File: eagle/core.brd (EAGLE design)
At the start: 41.9 x 19.7 mm, 28 parts, among them T1 BC846, T2 BC846, T3 BC846, T4 BC846

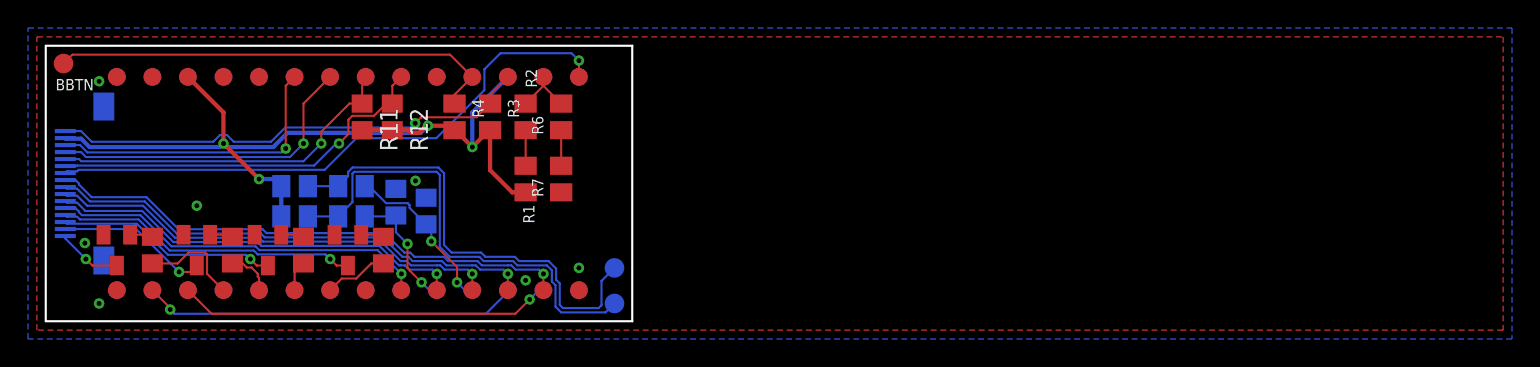
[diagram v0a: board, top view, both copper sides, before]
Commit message: Fixed ffc connector dimensions
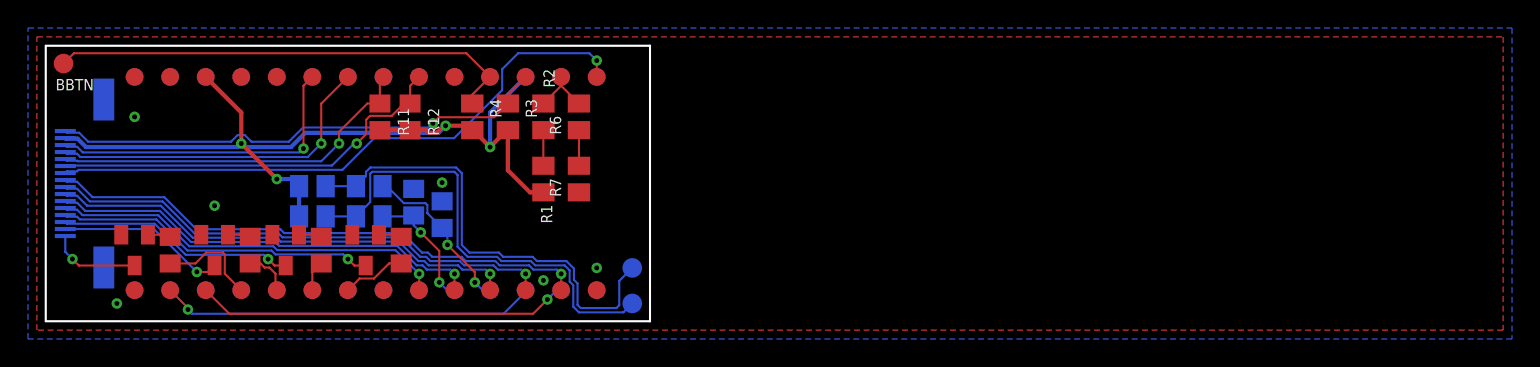
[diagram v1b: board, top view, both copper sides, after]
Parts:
- moved C2 1.27 mm to (26.3, 8.51)
- moved R1 1.27 mm to (35.6, 10.2)
- moved R2 1.27 mm to (35.6, 14.6)
- moved R3 1.27 mm to (33.0, 14.6)
- moved R6 1.27 mm to (38.1, 14.6)
- moved R7 1.27 mm to (38.1, 10.2)
- moved R15 1.27 mm to (8.89, 5.08)
- moved R10 1.27 mm to (23.1, 7.49)
- moved R11 1.27 mm to (23.9, 14.6)
- moved R12 1.27 mm to (26.0, 14.6)
- moved R16 1.27 mm to (14.6, 5.08)
- moved R17 1.27 mm to (19.7, 5.08)
- moved R18 1.27 mm to (25.4, 5.08)
- moved R4 1.27 mm to (30.5, 14.6)
- moved R5 1.27 mm to (23.1, 9.65)
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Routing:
- net L1-: track 4.66 -> 6.49 mm
- net BBTN: track 32.6 -> 33.9 mm
- net SDA: track 28.0 -> 29.3 mm
- net TFTCS: track 35.4 -> 36.6 mm
- net DC: track 32.6 -> 33.9 mm
- net L2-: track 10.9 -> 12.1 mm
- net SCL: track 25.5 -> 26.8 mm
- net LRCL: track 23.1 -> 24.4 mm
- net L4-: track 21.7 -> 23.0 mm
- net L3-: track 15.8 -> 17.0 mm
- net BCLK: track 21.5 -> 22.7 mm
- net SCK: track 42.5 -> 43.8 mm
- net PBTN: track 34.6 -> 35.9 mm
- net DOUT: track 29.9 -> 31.1 mm
- net 3V: track 63.1 -> 64.3 mm
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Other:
- board size 41.9 x 19.7 mm -> 43.2 x 19.7 mm

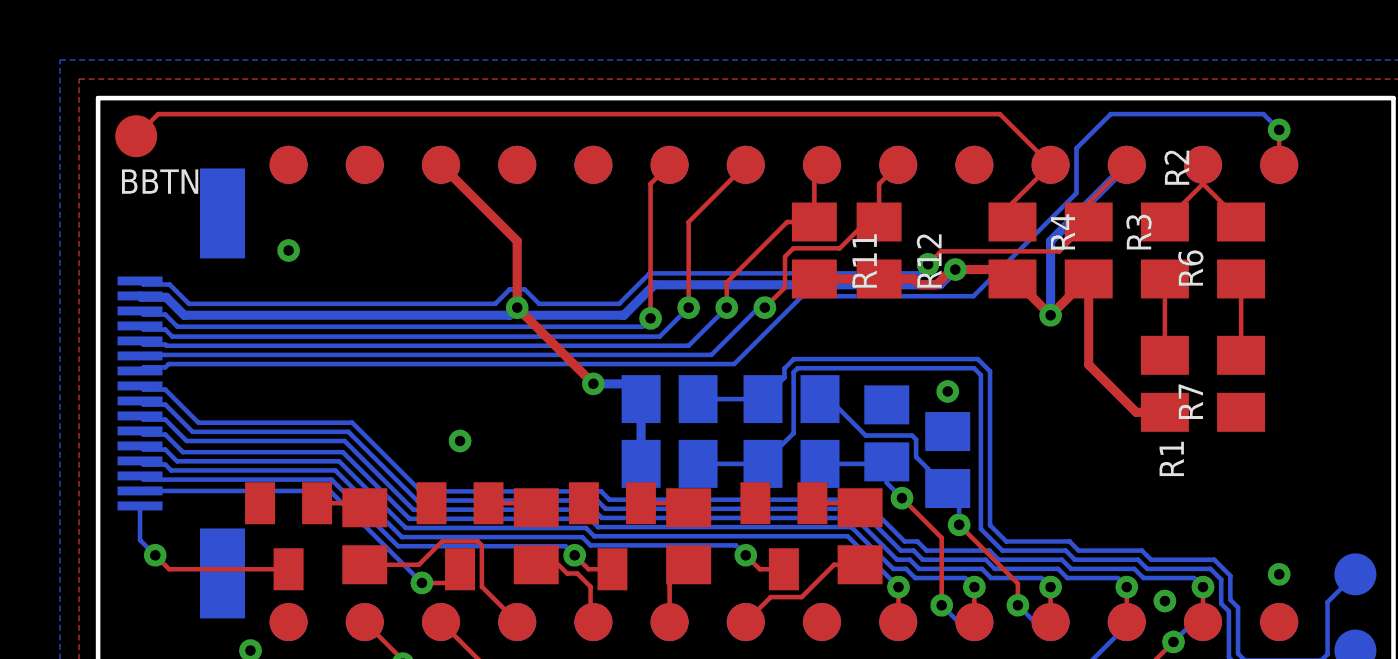
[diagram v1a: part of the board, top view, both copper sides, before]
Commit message: Added capacitor between 3v and gnd on core pcb
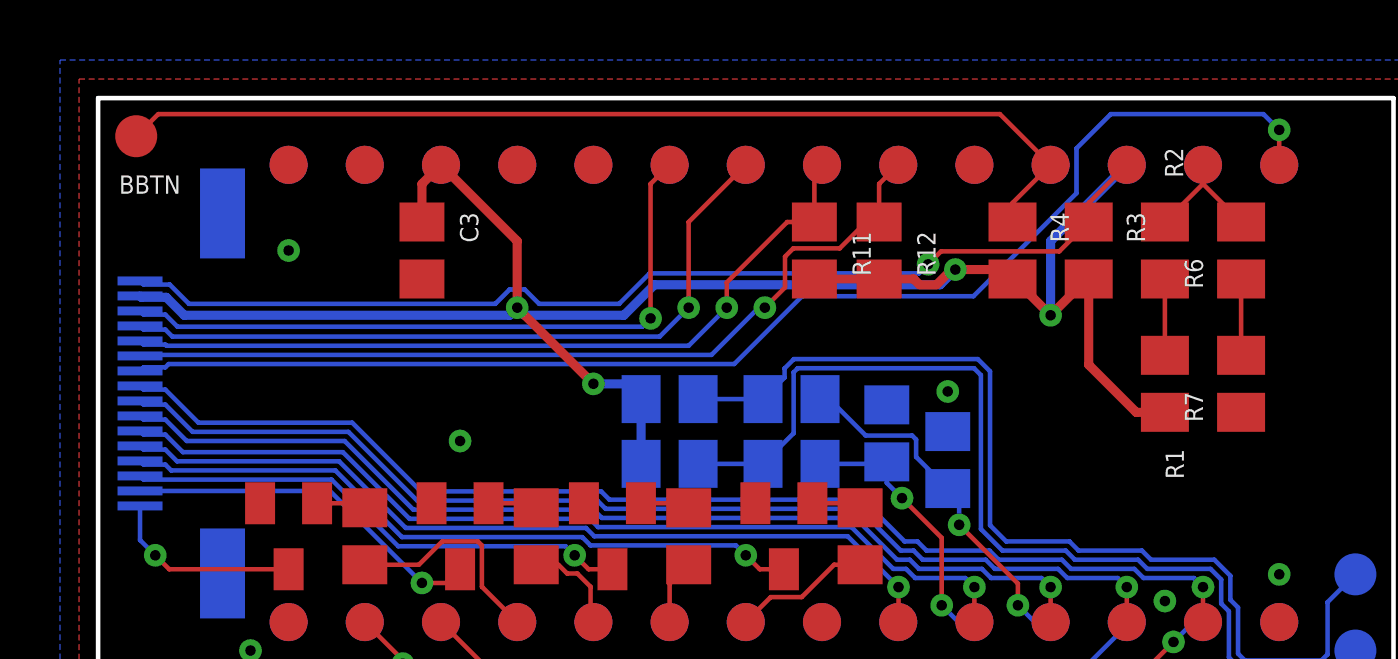
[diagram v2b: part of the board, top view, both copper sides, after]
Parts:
- added C3: 0.1u, resistor:C0805
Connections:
- net 3V: now also C3.1
- net GND: now also C3.2
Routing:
- net 3V: track 64.3 -> 66.5 mm
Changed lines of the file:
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@@
 <elements>
 <element name="R5" library="resistor" library_urn="urn:adsk.eagle:library:348" package="M0805" package3d_urn="urn:adsk.eagle:package:23556/2" value="10k" x="23.114" y="9.652" smashed="yes" rot="MR0">
-<attribute name="NAME" x="19.304" y="10.287" size="0.8128" layer="26" rot="MR180"/>
+<attribute name="NAME" x="19.304" y="10.287" size="0.6096" layer="26" rot="MR180"/>
 <attribute name="VALUE" x="24.384" y="7.112" size="1.27" layer="28" rot="MR0"/>
 </element>
 <element name="R8" library="resistor" library_urn="urn:adsk.eagle:library:348" package="M0805" package3d_urn="urn:adsk.eagle:package:23556/2" value="10k" x="19.05" y="9.652" smashed="yes" rot="MR0">
-<attribute name="NAME" x="19.685" y="10.922" size="0.8128" layer="26" rot="MR0"/>
+<attribute name="NAME" x="19.685" y="10.922" size="0.6096" layer="26" rot="MR0"/>
 <attribute name="VALUE" x="20.32" y="7.112" size="1.27" layer="28" rot="MR0"/>
 </element>
 <element name="R9" library="resistor" library_urn="urn:adsk.eagle:library:348" package="M0805" package3d_urn="urn:adsk.eagle:package:23556/2" value="10k" x="19.05" y="7.493" smashed="yes" rot="MR0">
-<attribute name="NAME" x="21.59" y="10.668" size="0.8128" layer="26" rot="MR180"/>
+<attribute name="NAME" x="21.59" y="10.668" size="0.6096" layer="26" rot="MR180"/>
 <attribute name="VALUE" x="20.32" y="4.953" size="1.27" layer="28" rot="MR0"/>
 </element>
 <element name="R10" library="resistor" library_urn="urn:adsk.eagle:library:348" package="M0805" package3d_urn="urn:adsk.eagle:package:23556/2" value="10k" x="23.114" y="7.493" smashed="yes" rot="MR0">
-<attribute name="NAME" x="24.384" y="11.303" size="0.8128" layer="26" rot="MR0"/>
+<attribute name="NAME" x="24.384" y="11.303" size="0.6096" layer="26" rot="MR0"/>
 <attribute name="VALUE" x="24.384" y="4.953" size="1.27" layer="28" rot="MR0"/>
 </element>
 <element name="C1" library="resistor" library_urn="urn:adsk.eagle:library:348" package="C0805" package3d_urn="urn:adsk.eagle:package:23617/2" value="0.1u" x="28.321" y="7.62" smashed="yes" rot="MR90">
-<attribute name="NAME" x="28.321" y="3.81" size="0.8128" layer="26" rot="MR90"/>
+<attribute name="NAME" x="28.321" y="3.81" size="0.6096" layer="26" rot="MR90"/>
 <attribute name="VALUE" x="25.781" y="6.35" size="1.27" layer="28" rot="MR90"/>
 </element>
 <element name="C2" library="resistor" library_urn="urn:adsk.eagle:library:348" package="C0805" package3d_urn="urn:adsk.eagle:package:23617/2" value="0.1u" x="26.289" y="8.509" smashed="yes" rot="MR90">
-<attribute name="NAME" x="26.289" y="5.969" size="0.8128" layer="26" rot="MR270"/>
+<attribute name="NAME" x="26.289" y="5.969" size="0.6096" layer="26" rot="MR270"/>
 <attribute name="VALUE" x="23.749" y="7.239" size="1.27" layer="28" rot="MR90"/>
 </element>
@@
 <element name="U$2" library="general" package="TEENSYSMALL" value="TEENSYSMALL" x="24.13" y="9.84" smashed="yes" rot="MR0"/>
 <element name="R1" library="resistor" library_urn="urn:adsk.eagle:library:348" package="M0805" package3d_urn="urn:adsk.eagle:package:23556/2" value="20M" x="35.56" y="10.16" smashed="yes" rot="R270">
-<attribute name="NAME" x="36.195" y="6.985" size="0.8128" layer="25" rot="R90"/>
+<attribute name="NAME" x="36.195" y="6.985" size="0.6096" layer="25" rot="R90"/>
 <attribute name="VALUE" x="33.02" y="11.43" size="1.27" layer="27" rot="R270"/>
 </element>
 <element name="R2" library="resistor" library_urn="urn:adsk.eagle:library:348" package="M0805" package3d_urn="urn:adsk.eagle:package:23556/2" value="20M" x="35.56" y="14.605" smashed="yes" rot="R270">
-<attribute name="NAME" x="35.56" y="18.034" size="0.8128" layer="25" rot="R270"/>
+<attribute name="NAME" x="35.56" y="18.034" size="0.6096" layer="25" rot="R270"/>
 <attribute name="VALUE" x="33.02" y="15.875" size="1.27" layer="27" rot="R270"/>
 </element>
@@
 <element name="U$3" library="general" package="16PINFFC" value="16PINFFC" x="1.397" y="9.84" smashed="yes" rot="MR90"/>
 <element name="R3" library="resistor" library_urn="urn:adsk.eagle:library:348" package="M0805" package3d_urn="urn:adsk.eagle:package:23556/2" value="20M" x="33.02" y="14.605" smashed="yes" rot="R270">
-<attribute name="NAME" x="34.29" y="15.875" size="0.8128" layer="25" rot="R270"/>
+<attribute name="NAME" x="34.29" y="15.875" size="0.6096" layer="25" rot="R270"/>
 <attribute name="VALUE" x="30.48" y="15.875" size="1.27" layer="27" rot="R270"/>
 </element>
 <element name="R4" library="resistor" library_urn="urn:adsk.eagle:library:348" package="M0805" package3d_urn="urn:adsk.eagle:package:23556/2" value="20M" x="30.48" y="14.605" smashed="yes" rot="R270">
-<attribute name="NAME" x="31.75" y="15.875" size="0.8128" layer="25" rot="R270"/>
+<attribute name="NAME" x="31.75" y="15.875" size="0.6096" layer="25" rot="R270"/>
 <attribute name="VALUE" x="27.94" y="15.875" size="1.27" layer="27" rot="R270"/>
 </element>
 <element name="R6" library="resistor" library_urn="urn:adsk.eagle:library:348" package="M0805" package3d_urn="urn:adsk.eagle:package:23556/2" value="20M" x="38.1" y="14.605" smashed="yes" rot="R90">
-<attribute name="NAME" x="36.83" y="13.335" size="0.8128" layer="25" rot="R90"/>
+<attribute name="NAME" x="36.83" y="13.335" size="0.6096" layer="25" rot="R90"/>
 <attribute name="VALUE" x="40.64" y="13.335" size="1.27" layer="27" rot="R90"/>
 </element>
 <element name="R7" library="resistor" library_urn="urn:adsk.eagle:library:348" package="M0805" package3d_urn="urn:adsk.eagle:package:23556/2" value="20M" x="38.1" y="10.16" smashed="yes" rot="R90">
-<attribute name="NAME" x="36.83" y="8.89" size="0.8128" layer="25" rot="R90"/>
+<attribute name="NAME" x="36.83" y="8.89" size="0.6096" layer="25" rot="R90"/>
 <attribute name="VALUE" x="40.64" y="8.89" size="1.27" layer="27" rot="R90"/>
 </element>
 <element name="BBTN" library="testpad" library_urn="urn:adsk.eagle:library:385" package="TP14R" package3d_urn="urn:adsk.eagle:package:27966/1" value="TPTP14R" x="1.27" y="18.415" smashed="yes">
-<attribute name="NAME" x="0.697" y="16.4981" size="0.8128" layer="25"/>
+<attribute name="NAME" x="0.697" y="16.4981" size="0.6096" layer="25"/>
 <attribute name="POPULARITY" value="0" x="1.27" y="18.415" size="1.778" layer="27" display="off"/>
 <attribute name="TP_SIGNAL_NAME" value="" x="1.27" y="18.415" size="1.778" layer="27" display="off"/>
@@
 </element>
 <element name="ENCR" library="testpad" library_urn="urn:adsk.eagle:library:385" package="TP14R" package3d_urn="urn:adsk.eagle:package:27966/1" value="TPTP14R" x="41.91" y="1.27" smashed="yes" rot="MR0">
-<attribute name="NAME" x="42.61" y="2.1471" size="0.8128" layer="26" rot="MR0"/>
+<attribute name="NAME" x="42.61" y="2.1471" size="0.6096" layer="26" rot="MR0"/>
 <attribute name="POPULARITY" value="0" x="41.91" y="1.27" size="1.778" layer="28" rot="MR0" display="off"/>
 <attribute name="TP_SIGNAL_NAME" value="" x="41.91" y="-1.27" size="1" layer="38" rot="MR0"/>
@@
 </element>
 <element name="ENCL" library="testpad" library_urn="urn:adsk.eagle:library:385" package="TP14R" package3d_urn="urn:adsk.eagle:package:27966/1" value="TPTP14R" x="41.91" y="3.81" smashed="yes" rot="MR0">
-<attribute name="NAME" x="42.61" y="4.8141" size="0.8128" layer="26" rot="MR0"/>
+<attribute name="NAME" x="42.61" y="4.8141" size="0.6096" layer="26" rot="MR0"/>
 <attribute name="POPULARITY" value="0" x="41.91" y="3.81" size="1.778" layer="28" rot="MR0" display="off"/>
 <attribute name="TP_SIGNAL_NAME" value="" x="41.91" y="1.27" size="1" layer="38" rot="MR0"/>
@@
 </element>
 <element name="R11" library="resistor" library_urn="urn:adsk.eagle:library:348" package="R0805" package3d_urn="urn:adsk.eagle:package:23553/2" value="" x="23.876" y="14.605" smashed="yes" rot="R270">
-<attribute name="NAME" x="25.146" y="15.24" size="0.8128" layer="25" rot="R270"/>
+<attribute name="NAME" x="25.146" y="15.24" size="0.6096" layer="25" rot="R270"/>
 <attribute name="VALUE" x="21.336" y="15.24" size="1.27" layer="27" rot="R270"/>
 </element>
 <element name="R12" library="resistor" library_urn="urn:adsk.eagle:library:348" package="R0805" package3d_urn="urn:adsk.eagle:package:23553/2" value="" x="26.035" y="14.605" smashed="yes" rot="R270">
-<attribute name="NAME" x="27.305" y="15.24" size="0.8128" layer="25" rot="R270"/>
+<attribute name="NAME" x="27.305" y="15.24" size="0.6096" layer="25" rot="R270"/>
 <attribute name="VALUE" x="23.495" y="15.24" size="1.27" layer="27" rot="R270"/>
+</element>
+<element name="C3" library="resistor" library_urn="urn:adsk.eagle:library:348" package="C0805" package3d_urn="urn:adsk.eagle:package:23617/2" value="0.1u" x="10.795" y="14.605" smashed="yes" rot="R270">
+<attribute name="NAME" x="12.065" y="15.875" size="0.6096" layer="25" rot="R270"/>
+<attribute name="VALUE" x="8.255" y="15.875" size="1.27" layer="27" rot="R270"/>
 </element>
 </elements>
@@
 <via x="6.35" y="14.605" extent="1-16" drill="0.35"/>
 <via x="28.321" y="9.906" extent="1-16" drill="0.35"/>
+<contactref element="C3" pad="2"/>
 </signal>
 <signal name="3V" class="1">
@@
 <wire x1="2.27325" y1="13.0448" x2="2.87205" y2="12.446" width="0.3048" layer="16"/>
 <wire x1="2.87205" y1="12.446" x2="13.716" y2="12.446" width="0.3048" layer="16"/>
+<contactref element="C3" pad="1"/>
+<wire x1="10.795" y1="15.555" x2="10.795" y2="16.825" width="0.3048" layer="1"/>
+<wire x1="10.795" y1="16.825" x2="11.43" y2="17.46" width="0.3048" layer="1"/>
 </signal>
 <signal name="ENCL">

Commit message: misc pcb changes
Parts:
- removed C1, C2: 0.1u, resistor:C0805
- removed R10, R5, R8, R9: 10k, resistor:M0805
- added GND: TPTP14R, testpad:TP14R
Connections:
- removed net ENCL: ENCL.TP, R5.2, R8.1
- removed net ENCR: ENCR.TP, R10.2, R9.1
- net 3V: no longer R8.2, R9.2
- net ENCPINL: now also ENCL.TP; no longer C1.1, R5.1
- net ENCPINR: now also ENCR.TP; no longer C2.1, R10.1
- net GND: now also GND.TP; no longer C1.2, C2.2
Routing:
- net ENCL: track 33.4 -> 0.00 mm
- net ENCR: track 33.2 -> 0.00 mm
- net ENCPINR: track 9.11 -> 17.4 mm, vias 2 -> 0
- net 3V: track 66.5 -> 59.0 mm, vias 4 -> 2
- net ENCPINL: track 12.0 -> 14.8 mm, vias 2 -> 0
- net TFTRST: track 28.4 -> 30.1 mm
- net MOSI: track 39.4 -> 40.7 mm
- net TFTCS: track 36.6 -> 38.0 mm
- net DC: track 33.9 -> 35.1 mm
- net DOUT: track 31.1 -> 32.1 mm
- net SCK: track 43.8 -> 43.3 mm, vias 1 -> 3

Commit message: all the things
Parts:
- removed R15, R16, R17, R18: (no value), resistor:R0805
- removed T1, T2, T3, T4: BC846, transistor:SOT23
- added SPGND, SPSCL, SPSDA, SPV: TPTP14R, testpad:TP14R
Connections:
- removed net N$2: R15.2, T1.1
- removed net N$3: R16.2, T2.1
- removed net N$4: R17.2, T3.1
- removed net N$5: R18.2, T4.1
- removed net PWM1: R15.1, U$1.2
- removed net PWM2: R16.1, U$1.3
- removed net PWM3: R17.1, U$1.4
- removed net PWM4: R18.1, U$1.5
- net 3V: now also SPV.TP
- net GND: now also SPGND.TP; no longer T1.2, T2.2, T3.2, T4.2
- net L1-: now also U$1.2; no longer T1.3
- net L2-: now also U$1.3; no longer T2.3
- net L3-: now also U$1.4; no longer T3.3
- net L4-: now also U$1.5; no longer T4.3
- net SCL: now also SPSCL.TP
- net SDA: now also SPSDA.TP
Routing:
- net 3V: track 59.0 -> 75.4 mm
- net SDA: track 29.3 -> 38.0 mm, vias 1 -> 2
- net L1-: track 6.49 -> 14.2 mm
- net PWM1: track 7.32 -> 0.00 mm
- net SCL: track 26.8 -> 33.6 mm, vias 1 -> 2
- net L2-: track 12.1 -> 16.9 mm
- net PWM4: track 4.60 -> 0.00 mm
- net PWM2: track 3.33 -> 0.00 mm
- net L3-: track 17.0 -> 19.7 mm
- net PWM3: track 2.17 -> 0.00 mm
- net N$2: track 1.65 -> 0.00 mm
- net N$5: track 1.65 -> 0.00 mm
- net N$4: track 1.65 -> 0.00 mm
- net N$3: track 1.65 -> 0.00 mm
- net L4-: track 23.0 -> 22.4 mm

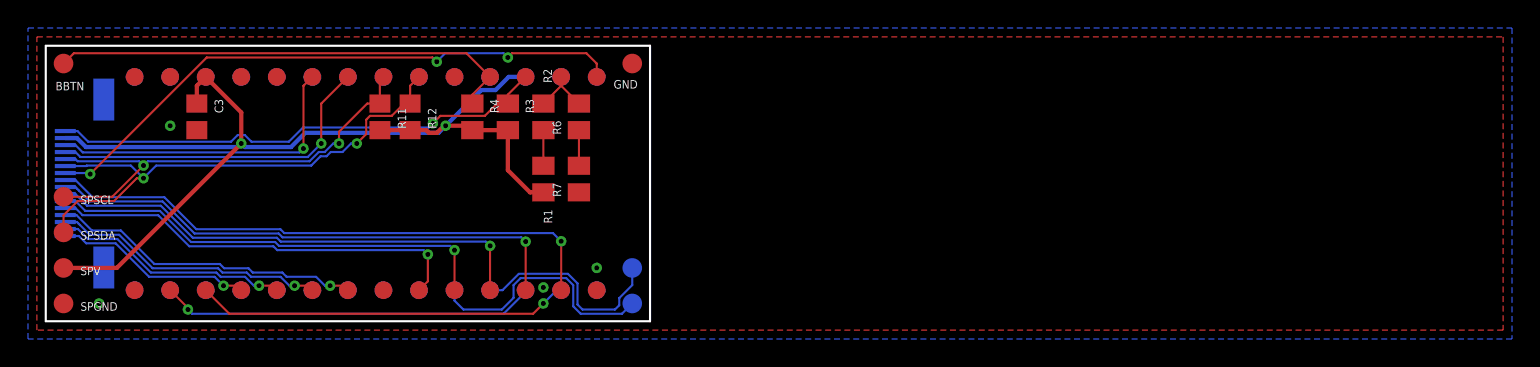
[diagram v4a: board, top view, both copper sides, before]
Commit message: core is now 18mm
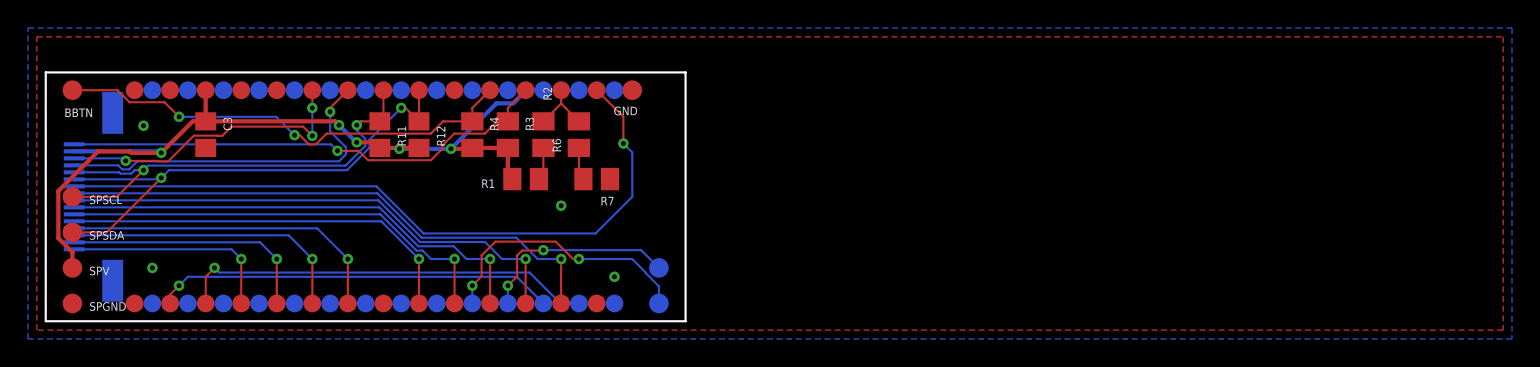
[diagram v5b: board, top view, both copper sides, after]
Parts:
- moved BBTN 2.01 mm to (1.91, 16.5)
- moved ENCL 1.91 mm to (43.8, 3.81)
- moved ENCR 1.91 mm to (43.8, 1.27)
- moved GND 1.90 mm to (41.9, 16.5)
- moved U$2 1.59 mm to (25.4, 8.89)
- moved R12 1.42 mm to (26.7, 13.3)
- moved C3 1.42 mm to (11.4, 13.3)
- moved R1 1.27 mm to (34.3, 10.2), turned to 180 degrees
- moved R11 1.27 mm to (23.9, 13.3)
- moved R2 1.27 mm to (35.6, 13.3)
- moved R3 1.27 mm to (33.0, 13.3)
- moved R4 1.27 mm to (30.5, 13.3)
- moved R6 1.27 mm to (38.1, 13.3)
- moved R7 1.27 mm to (39.4, 10.2), turned to 180 degrees
- moved U$3 1.14 mm to (2.03, 8.89)
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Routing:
- net 3V: track 75.4 -> 61.6 mm, vias 2 -> 5
- net SCK: track 43.3 -> 51.0 mm, vias 3 -> 1
- net T4TX: track 26.9 -> 29.9 mm
- net ENCPINR: track 17.4 -> 19.4 mm, vias 0 -> 2
- net T4RX: track 26.9 -> 28.6 mm
- net L1-: track 14.2 -> 15.4 mm
- net L4-: track 22.4 -> 23.6 mm
- net L3-: track 19.7 -> 20.9 mm
- net L2-: track 16.9 -> 18.1 mm
- net LRCL: track 24.4 -> 25.6 mm
- net TFTRST: track 30.1 -> 28.9 mm
- net BCLK: track 22.7 -> 21.7 mm, vias 1 -> 3
- net MOSI: track 40.7 -> 39.9 mm
- net TFTCS: track 38.0 -> 37.2 mm
- net DC: track 35.1 -> 34.4 mm
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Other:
- board size 43.2 x 19.7 mm -> 45.7 x 17.8 mm
